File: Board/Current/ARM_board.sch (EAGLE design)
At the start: 180 parts, among them IC3 STM32F437VI, IC4 LM358DT, J1 USART/I2C, J10 ANALOG, J11 DGND, J12 DPWR, J13 DIGITAL, J14 SGND, J15 SPWR, J16 SERVO, J2 I2C2/USART3, J3 USART2, J5 SPI, J6 Bluesmirf, J7 SWD, J8 AGND, J9 APWR, Q1 STL4P2UH7, Q2 2STR1230, Q3 STL4P2UH7, SW1 SW, U1 LSM330, U10 BAV99, U11 BAV99, U12 USBLC6-2, U13 USBLC6-2, U14 STMPS2171MTR, U15 MC74HC164, U3 NC7SZU04, U4 L6206Q, U5 L6206Q, U6 SI7617, U7 SI7617, U8 SI7617, U9 SI7617, Y2 8MHz

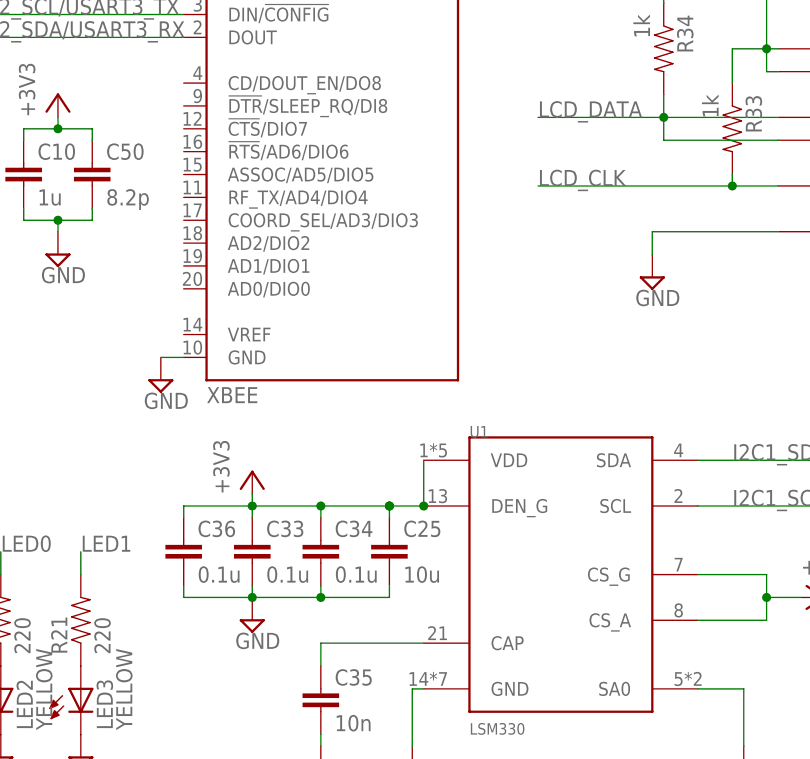
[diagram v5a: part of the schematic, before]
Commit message: Cleaned up the layout around the gyro a bit.
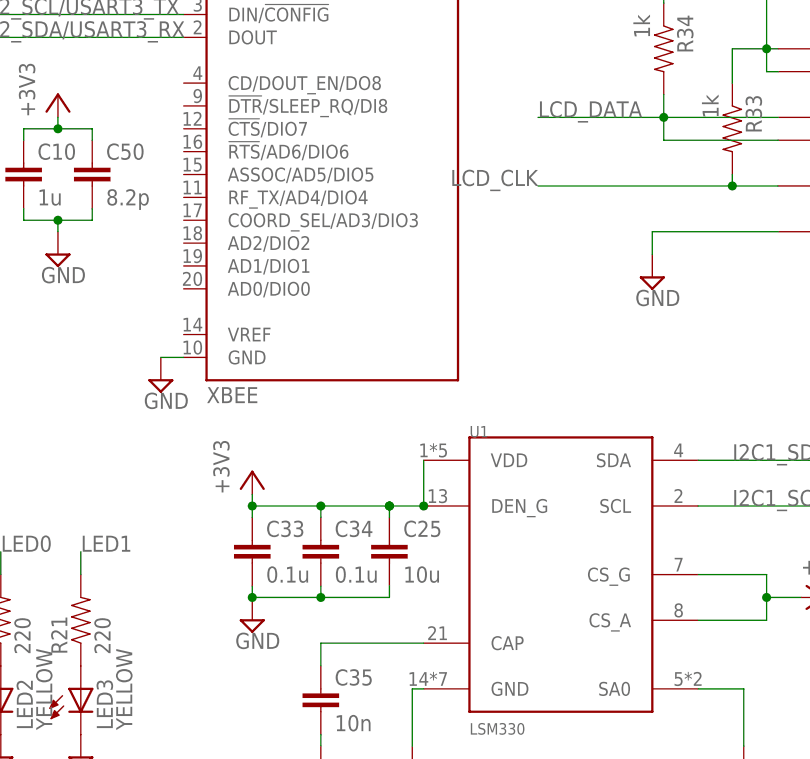
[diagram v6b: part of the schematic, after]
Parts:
- removed C36: 0.1u, SparkFun:CAP0402-CAP
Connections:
- net +3V3: no longer C36.1
- net GND: no longer C36.2
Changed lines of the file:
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@@
 <setting verticaltext="up"/>
 </settings>
-<grid distance="0.05" unitdist="inch" unit="inch" style="lines" multiple="1" display="no" altdistance="0.01" altunitdist="inch" altunit="inch"/>
+<grid distance="0.1" unitdist="inch" unit="inch" style="lines" multiple="1" display="no" altdistance="0.01" altunitdist="inch" altunit="inch"/>
 <layers>
 <layer number="1" name="Top" color="4" fill="1" visible="no" active="no"/>
@@
 <part name="R53" library="SparkFun" deviceset="RESISTOR" device="0402-RES" value="330k"/>
 <part name="C33" library="SparkFun" deviceset="CAP" device="0402-CAP" value="0.1u"/>
-<part name="C36" library="SparkFun" deviceset="CAP" device="0402-CAP" value="0.1u"/>
 </parts>
 <sheets>
@@
 <instance part="R53" gate="G$1" x="80.01" y="233.68"/>
 <instance part="C33" gate="G$1" x="261.62" y="82.55"/>
-<instance part="C36" gate="G$1" x="254" y="82.55"/>
 </instances>
 <busses>
@@
 <pinref part="C34" gate="G$1" pin="2"/>
 <wire x1="269.24" y1="80.01" x2="269.24" y2="78.74" width="0.1524" layer="91"/>
-<pinref part="C36" gate="G$1" pin="2"/>
-<wire x1="261.62" y1="78.74" x2="254" y2="78.74" width="0.1524" layer="91"/>
-<wire x1="254" y1="78.74" x2="254" y2="80.01" width="0.1524" layer="91"/>
 <junction x="261.62" y="78.74"/>
 <junction x="269.24" y="78.74"/>
@@
 <wire x1="269.24" y1="88.9" x2="261.62" y2="88.9" width="0.1524" layer="91"/>
 <wire x1="261.62" y1="88.9" x2="261.62" y2="87.63" width="0.1524" layer="91"/>
-<pinref part="C36" gate="G$1" pin="1"/>
-<wire x1="261.62" y1="88.9" x2="254" y2="88.9" width="0.1524" layer="91"/>
-<wire x1="254" y1="88.9" x2="254" y2="87.63" width="0.1524" layer="91"/>
 <junction x="261.62" y="88.9"/>
 <junction x="269.24" y="88.9"/>
@@
 <pinref part="U15" gate="G$1" pin="CLK"/>
 <wire x1="320.04" y1="124.46" x2="314.96" y2="124.46" width="0.1524" layer="91"/>
-<label x="293.37" y="124.46" size="1.778" layer="95"/>
+<label x="293.37" y="124.46" size="1.778" layer="95" rot="MR0"/>
 <pinref part="R33" gate="G$1" pin="2"/>
 <wire x1="314.96" y1="124.46" x2="293.37" y2="124.46" width="0.1524" layer="91"/>

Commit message: Cleaned up the part numbers of everything but the resistors/caps.
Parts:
- removed IC3: STM32F437VI, new_parts:STM32F407VET
- removed JP2: DPWR_SEL, SparkFun:JUMPER-3PTH
- removed JP3: MISC, SparkFun:M081X08
- removed U$1: PM6685, r_cubed:PM6685
- removed U$2: DUAL-MOSFET, r_cubed:DUAL-MOSFET
- removed U$5: LD1117V33, r_cubed:LD1117
- removed U13: USBLC6-2, new_parts:USBLC6-2
- removed U14: STMPS2171MTR, r_cubed:RT9715
- removed U15: MC74HC164, r_cubed:MC74HC164
- added D4, D5: BAV99, Parts:BAV99
- added J17: SERVO, SparkFun:M081X08
- added J4: I2C2/USART3, SparkFun:M04PTH
- added Q5, Q6: STL4P2UH7, r_cubed:STL4P2UH7
- added Q7, Q8: SI7617, r_cubed:SI7617
- added Q9: 2STR1230, SparkFun:TRANSISTOR_NPNSOT23-3
- D1: value STPS1L30M -> SOD-23; device SparkFun:DIODE-SCHOTTKYA -> r_cubed:SOD-23
- D3: value SOD-23 -> STPS1L30M; device r_cubed:SOD-23 -> SparkFun:DIODE-SCHOTTKYA
- J1: value USART/I2C -> Bluesmirf; device SparkFun:M04PTH -> SparkFun:M06SIP
- J10: value ANALOG -> APWR
- J11: value DGND -> ANALOG; device SparkFun:M15 -> SparkFun:M081X08
- J12: value DPWR -> DGND
- J13: value DIGITAL -> DPWR
- J14: value SGND -> DIGITAL; device SparkFun:M081X08 -> SparkFun:M15
- J15: value SPWR -> SGND
- J16: value SERVO -> SPWR
- J2: value I2C2/USART3 -> I2C1
- J3: value USART2 -> USART/I2C
- J6: value Bluesmirf -> USART2; device SparkFun:M06SIP -> SparkFun:M04PTH
- J8: value AGND -> MISC
- J9: value APWR -> AGND
- JP1: value I2C1 -> DPWR_SEL; device SparkFun:M04PTH -> SparkFun:JUMPER-3PTH
- Q1: value STL4P2UH7 -> SI7617; device r_cubed:STL4P2UH7 -> r_cubed:SI7617
- Q2: value 2STR1230 -> SI7617; device SparkFun:TRANSISTOR_NPNSOT23-3 -> r_cubed:SI7617
- Q3: value STL4P2UH7 -> DUAL-MOSFET; device r_cubed:STL4P2UH7 -> r_cubed:DUAL-MOSFET
- U1: value LSM330 -> PM6685; device r_cubed:LSM330 -> r_cubed:PM6685
- U10: value BAV99 -> STM32F437VI; device Parts:BAV99 -> new_parts:STM32F407VET
- U11: value BAV99 -> LSM330; device Parts:BAV99 -> r_cubed:LSM330
- U12: value USBLC6-2 -> MC74HC164; device new_parts:USBLC6-2 -> r_cubed:MC74HC164
- U3: value NC7SZU04 -> LD1117V33; device SparkFun:INVERTER"" -> r_cubed:LD1117
- U4: value L6206Q -> USBLC6-2; device r_cubed:L6206Q -> new_parts:USBLC6-2
- U5: value L6206Q -> STMPS2171MTR; device r_cubed:L6206Q -> r_cubed:RT9715
- U6: value SI7617 -> USBLC6-2; device r_cubed:SI7617 -> new_parts:USBLC6-2
- U7: value SI7617 -> NC7SZU04; device r_cubed:SI7617 -> SparkFun:INVERTER""
- U8, U9: value SI7617 -> L6206Q; device r_cubed:SI7617 -> r_cubed:L6206Q
- renumbered IC4 to U2, L3 to L2, LED2 to D9, LED3 to D10, LED4 to D8, LED5 to D11, LED6 to D7, LED7 to D6, SD to USD, SG1 to LS1, U$4 to Q4, Y2 to Y1
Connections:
- net +3V3: now also J1.5, J10.1, J10.2, J10.3, J10.4, J10.5, J10.6, J10.7, J10.8, J4.4, J6.4, JP1.1, U1.OUT3, U10BAT_AN.VBAT, U10BAT_AN.VDDA, U10BAT_AN.VDD_6, U10BAT_AN.VREF+, U10POWER.VDD_1, U10POWER.VDD_2, U10POWER.VDD_3, U10POWER.VDD_4, U10POWER.VDD_5, U11.CS_A, U11.CS_G, U11.DEN_G, U11.VDD, U12./RST, U12.VCC, U3.VOUT, U4.VBUS, U6.VBUS; no longer IC3BAT_AN.VBAT, IC3BAT_AN.VDDA, IC3BAT_AN.VDD_6, IC3BAT_AN.VREF+, IC3POWER.VDD_1, IC3POWER.VDD_2, IC3POWER.VDD_3, IC3POWER.VDD_4, IC3POWER.VDD_5, J1.4, J6.5, J9.1, J9.2, J9.3, J9.4, J9.5, J9.6, J9.7, J9.8, JP1.4, JP2.1, U$1.OUT3, U$5.VOUT, U1.CS_A, U1.CS_G, U1.DEN_G, U1.VDD, U12.VBUS, U13.VBUS, U15./RST, U15.VCC
- net 5V: now also J8.6, JP1.3, Q5.S, Q6.S, Q7.D, U1.OUT5, U5.VIN, U7.VCC; no longer JP2.3, JP3.6, Q1.S, Q3.S, U$1.OUT5, U14.VIN, U3.VCC, U9.D
- net ANALOG0: now also J11.1, U10PORTA_L.PA3; no longer IC3PORTA_L.PA3, J10.1
- net ANALOG1: now also J11.2, U10PORTA_L.PA2; no longer IC3PORTA_L.PA2, J10.2
- net ANALOG2: now also J11.3, U10PORTA_L.PA1; no longer IC3PORTA_L.PA1, J10.3
- net ANALOG3: now also J11.4, U10PORTA_L.PA0; no longer IC3PORTA_L.PA0, J10.4
- net ANALOG4: now also J11.5, U10PORTC_L.PC3; no longer IC3PORTC_L.PC3, J10.5
- net ANALOG5: now also J11.6, U10PORTC_L.PC2; no longer IC3PORTC_L.PC2, J10.6
- net ANALOG6: now also J11.7, U10PORTC_L.PC1; no longer IC3PORTC_L.PC1, J10.7
- net ANALOG7: now also J11.8, U10PORTC_L.PC0; no longer IC3PORTC_L.PC0, J10.8
- net ANALOG8: now also J8.3, U10PORTB_L.PB1; no longer IC3PORTB_L.PB1, JP3.3
- net ANALOG9: now also J8.4, U10PORTB_L.PB0; no longer IC3PORTB_L.PB0, JP3.4
- net BAT_SENSE: now also U10PORTC_L.PC4; no longer IC3PORTC_L.PC4
- net BOOT1: now also U10PORTB_L.PB2; no longer IC3PORTB_L.PB2
- net BOOT3: now also D1.P$2; no longer D3.P$2
- net BTN0: now also U10PORTD_H.PD10; no longer IC3PORTD_H.PD10
- net BTN1: now also U10PORTD_H.PD11; no longer IC3PORTD_H.PD11
- net BUZZER: now also U10PORTA_L.PA4; no longer IC3PORTA_L.PA4
- net DIGITAL0: now also J14.1, U10PORTC_H.PC15; no longer IC3PORTC_H.PC15, J13.1
- net DIGITAL1: now also J14.2, U10PORTC_H.PC14; no longer IC3PORTC_H.PC14, J13.2
- net DIGITAL10: now also J14.11, U10PORTB_L.PB5; no longer IC3PORTB_L.PB5, J13.11
- net DIGITAL11: now also J14.12, U10PORTB_L.PB4; no longer IC3PORTB_L.PB4, J13.12
- net DIGITAL12: now also J14.13, U10PORTB_L.PB3; no longer IC3PORTB_L.PB3, J13.13
- net DIGITAL13: now also J14.14, U10PORTD_L.PD7; no longer IC3PORTD_L.PD7, J13.14
- net DIGITAL14: now also J14.15, U10PORTD_L.PD3; no longer IC3PORTD_L.PD3, J13.15
- net DIGITAL15: now also J8.1, U10PORTE_H.PE13; no longer IC3PORTE_H.PE13, JP3.1
- net DIGITAL16: now also J8.2, U10PORTE_H.PE14; no longer IC3PORTE_H.PE14, JP3.2
- net DIGITAL2: now also J14.3, U10PORTC_H.PC13; no longer IC3PORTC_H.PC13, J13.3
- net DIGITAL3: now also J14.4, U10PORTE_L.PE6; no longer IC3PORTE_L.PE6, J13.4
- net DIGITAL4: now also J14.5, U10PORTE_L.PE5; no longer IC3PORTE_L.PE5, J13.5
- net DIGITAL5: now also J14.6, U10PORTE_L.PE4; no longer IC3PORTE_L.PE4, J13.6
- net DIGITAL6: now also J14.7, U10PORTE_L.PE3; no longer IC3PORTE_L.PE3, J13.7
- net DIGITAL7: now also J14.8, U10PORTE_L.PE2; no longer IC3PORTE_L.PE2, J13.8
- net DIGITAL8: now also J14.9, U10PORTE_L.PE1; no longer IC3PORTE_L.PE1, J13.9
- net DIGITAL9: now also J14.10, U10PORTE_L.PE0; no longer IC3PORTE_L.PE0, J13.10
- net GND: now also D3.A, J1.4, J12.1, J12.10, J12.11, J12.12, J12.13, J12.14, J12.15, J12.2, J12.3, J12.4, J12.5, J12.6, J12.7, J12.8, J12.9, J15.1, J15.2, J15.3, J15.4, J15.5, J15.6, J15.7, J15.8, J4.3, J6.3, J9.1, J9.2, J9.3, J9.4, J9.5, J9.6, J9.7, J9.8, Q3.S2, Q9.E, U1.LDO3SEL, U1.PGND, U1.SGND, U1.SGND2, U1.SKIP, U1.V5SW, U10BAT_AN.VSSA, U10POWER.VSS_2, U10POWER.VSS_4, U10POWER.VSS_5, U10POWER.VSS_6, U11.GND, U11.SA0, U6.GND, U7.GND, U8.GND, U8.PROGCLA, U8.PROGCLB, U8.SENSE_A, U8.SENSE_B, U9.GND, U9.PROGCLA, U9.PROGCLB, U9.SENSE_A, U9.SENSE_B; no longer D1.A, IC3BAT_AN.VSSA, IC3POWER.VSS_2, IC3POWER.VSS_4, IC3POWER.VSS_5, IC3POWER.VSS_6, J1.3, J11.1, J11.10, J11.11, J11.12, J11.13, J11.14, J11.15, J11.2, J11.3, J11.4, J11.5, J11.6, J11.7, J11.8, J11.9, J14.1, J14.2, J14.3, J14.4, J14.5, J14.6, J14.7, J14.8, J6.4, J8.1, J8.2, J8.3, J8.4, J8.5, J8.6, J8.8, JP1.3, JP3.7, Q2.E, U$1.LDO3SEL, U$1.PGND, U$1.SGND, U$1.SGND2, U$1.SKIP, U$1.V5SW, U$2.S2, U$5.GND, U1.GND, U1.SA0, U13.GND, U14.GND, U15.GND, U4.PROGCLA, U4.PROGCLB, U4.SENSE_A, U4.SENSE_B, U5.PROGCLA, U5.PROGCLB, U5.SENSE_A, U5.SENSE_B
- net I2C1_SCL: now also J2.1, U10PORTB_H.PB8, U11.SCL; no longer IC3PORTB_H.PB8, JP1.1, U1.SCL
- net I2C1_SDA: now also J2.2, U10PORTB_H.PB9, U11.SDA; no longer IC3PORTB_H.PB9, JP1.2, U1.SDA
- net I2C2_SCL/USART3_TX: now also J3.1, J4.1, U10PORTB_H.PB10; no longer IC3PORTB_H.PB10, J1.1, J2.1
- net I2C2_SDA/USART3_RX: now also J3.2, J4.2, U10PORTB_H.PB11; no longer IC3PORTB_H.PB11, J1.2, J2.2
- net LCD_CLK: now also U10PORTA_H.PA10, U12.CLK; no longer IC3PORTA_H.PA10, U15.CLK
- net LCD_DATA: now also U10PORTA_H.PA8, U12.A1, U12.A2; no longer IC3PORTA_H.PA8, U15.A1, U15.A2
- net LCD_E: now also U10PORTD_L.PD0; no longer IC3PORTD_L.PD0
- net LCD_RS: now also U10PORTD_L.PD1; no longer IC3PORTD_L.PD1
- net LDO5: now also D1.P$0, U1.FSEL, U1.LDO5; no longer D3.P$0, U$1.FSEL, U$1.LDO5
- net LED0: now also U10PORTE_H.PE15; no longer IC3PORTE_H.PE15
- net LED1: now also U10PORTD_L.PD4; no longer IC3PORTD_L.PD4
- net M0_A: now also U10PORTE_L.PE7, U8.IN1A, U8.IN1B; no longer IC3PORTE_L.PE7, U4.IN1A, U4.IN1B
- net M0_B: now also U10PORTE_H.PE8, U8.IN2A, U8.IN2B; no longer IC3PORTE_H.PE8, U4.IN2A, U4.IN2B
- net M0_EN: now also U10PORTE_H.PE9, U8.ENA, U8.ENB; no longer IC3PORTE_H.PE9, U4.ENA, U4.ENB
- net M0_FAULT: now also U10PORTD_H.PD8, U8.FAULT_A, U8.FAULT_B; no longer IC3PORTD_H.PD8, U4.FAULT_A, U4.FAULT_B
- net M1_A: now also U10PORTE_H.PE10, U9.IN1A, U9.IN1B; no longer IC3PORTE_H.PE10, U5.IN1A, U5.IN1B
- net M1_B: now also U10PORTE_H.PE12, U9.IN2A, U9.IN2B; no longer IC3PORTE_H.PE12, U5.IN2A, U5.IN2B
- net M1_EN: now also U10PORTE_H.PE11, U9.ENA, U9.ENB; no longer IC3PORTE_H.PE11, U5.ENA, U5.ENB
- net M1_FAULT: now also U10PORTD_H.PD9, U9.FAULT_A, U9.FAULT_B; no longer IC3PORTD_H.PD9, U5.FAULT_A, U5.FAULT_B
- net N$1: now also Q1.D; no longer U6.D
- net N$11: now also U11.CAP; no longer U1.CAP
- net N$13: now also U4.IO2_1; no longer U12.IO2_1
- net N$14: now also Q5.G, Q6.G; no longer Q1.G, Q3.G
- net N$15: now also U1.VCC; no longer U$1.VCC
- net N$16: now also U4.IO1_1; no longer U12.IO1_1
- net N$17: now also U6.IO1_1; no longer U13.IO1_1
- net N$19: now also J13.1, J13.10, J13.11, J13.12, J13.13, J13.14, J13.15, J13.2, J13.3, J13.4, J13.5, J13.6, J13.7, J13.8, J13.9, JP1.2; no longer J12.1, J12.10, J12.11, J12.12, J12.13, J12.14, J12.15, J12.2, J12.3, J12.4, J12.5, J12.6, J12.7, J12.8, J12.9, JP2.2
- net N$2: now also Q1.G; no longer U6.G
- net N$20: now also U1.BOOT5; no longer U$1.BOOT5
- net N$21: now also U5.VOUT; no longer U14.VOUT
- net N$22: now also Q6.D, U3.VIN; no longer Q3.D, U$5.VIN
- net N$23: now also Q1.S, Q2.S; no longer U6.S, U7.S
- net N$24: now also U10POWER.VCAP_1; no longer IC3POWER.VCAP_1
- net N$25: now also D1.P$1; no longer D3.P$1
- net N$27: now also U7.A; no longer U3.A
- net N$28: now also Q9.C; no longer Q2.C
- net N$3: now also U10RESET.BOOT0; no longer IC3RESET.BOOT0
- net N$30: now also U7.Y; no longer U3.Y
- net N$32: now also Q5.D; no longer Q1.D
- net N$33: now also U6.IO2_2; no longer U13.IO2_2
- net N$34: now also U4.IO2_2; no longer U12.IO2_2
- net N$36: now also U4.IO1_2; no longer U12.IO1_2
- net N$38: now also U9.VCP; no longer U5.VCP
- net N$39: now also D5.3, U9.VBOOT; no longer U10.3, U5.VBOOT
- net N$4: now also U10BAT_AN.VCAP_2; no longer IC3BAT_AN.VCAP_2
- net N$40: now also D5.2; no longer U10.2
- net N$44: now also U1.LGATE3; no longer U$1.LGATE3
- net N$45: now also U8.VCP; no longer U4.VCP
- net N$46: now also U10OSC.OSC_IN; no longer IC3OSC.OSC_IN
- net N$47: now also U10OSC.OSC_OUT; no longer IC3OSC.OSC_OUT
- net N$48: now also D4.3, U8.VBOOT; no longer U11.3, U4.VBOOT
- net N$49: now also D4.2; no longer U11.2
- net N$50: now also Q7.G; no longer U9.G
- net N$53: now also Q8.G; no longer U8.G
- net N$55: now also U1.CSENSE5; no longer U$1.CSENSE5
- net N$56: now also Q3.G1, U1.HGATE5; no longer U$1.HGATE5, U$2.G1
- net N$57: now also Q3.G2, U1.LGATE5; no longer U$1.LGATE5, U$2.G2
- net N$58: now also U12.QA; no longer U15.QA
- net N$59: now also U1.BOOT3; no longer U$1.BOOT3
- net N$6: now also U6.IO1_2; no longer U13.IO1_2
- net N$60: now also U12.QB; no longer U15.QB
- net N$61: now also U12.QC; no longer U15.QC
- net N$62: now also U12.QD; no longer U15.QD
- net N$63: now also U12.QE; no longer U15.QE
- net N$64: now also U12.QF; no longer U15.QF
- net N$65: now also Q9.B; no longer Q2.B
- net N$66: now also D2.C, Q3.S1, U1.PHASE5; no longer D1.C, U$1.PHASE5, U$2.S1
- net N$68: now also Q2.G; no longer U7.G
- net N$69: now also U1.COMP5; no longer U$1.COMP5
- net N$7: now also U1.VREF; no longer U$1.VREF
- net N$70: now also U12.QG; no longer U15.QG
- net N$71: now also U12.QH; no longer U15.QH
- net N$73: now also U1.HGATE3; no longer U$1.HGATE3
- net N$75: now also D3.C, U1.PHASE3; no longer D2.C, U$1.PHASE3
- net N$76: now also U1.CSENSE3; no longer U$1.CSENSE3
- net N$77: now also U1.COMP3; no longer U$1.COMP3
- net N$79: now also U1.VIN; no longer U$1.VIN
- net N$8: now also U6.IO2_1; no longer U13.IO2_1
- net N$82: now also U1.SHUDN; no longer U$1.SHUDN
- net N$83: now also U1.EN3; no longer U$1.EN3
- net N$84: now also U1.EN5; no longer U$1.EN5
- net OUT1: now also U8.OUT1A, U8.OUT1B; no longer U4.OUT1A, U4.OUT1B
- net OUT2: now also U8.OUT2A, U8.OUT2B; no longer U4.OUT2A, U4.OUT2B
- net OUT3: now also U9.OUT1A, U9.OUT1B; no longer U5.OUT1A, U5.OUT1B
- net OUT4: now also U9.OUT2A, U9.OUT2B; no longer U5.OUT2A, U5.OUT2B
- net RAW_SPWR: now also Q8.D; no longer U8.D
- net RESET: now also J8.5, U10RESET.NRST; no longer IC3RESET.NRST, JP3.5
- net SERVO0: now also J17.8, U10PORTD_H.PD12; no longer IC3PORTD_H.PD12, J16.8
- net SERVO1: now also J17.7, U10PORTD_H.PD13; no longer IC3PORTD_H.PD13, J16.7
- net SERVO2: now also J17.6, U10PORTD_H.PD14; no longer IC3PORTD_H.PD14, J16.6
- net SERVO3: now also J17.5, U10PORTD_H.PD15; no longer IC3PORTD_H.PD15, J16.5
- net SERVO4: now also J17.4, U10PORTC_L.PC6; no longer IC3PORTC_L.PC6, J16.4
- net SERVO5: now also J17.3, U10PORTC_L.PC7; no longer IC3PORTC_L.PC7, J16.3
- net SERVO6: now also J17.2, U10PORTC_H.PC8; no longer IC3PORTC_H.PC8, J16.2
- net SERVO7: now also J17.1, U10PORTC_H.PC9; no longer IC3PORTC_H.PC9, J16.1
- net SERVO_SENSE: now also U10PORTC_L.PC5; no longer IC3PORTC_L.PC5
- net SPI1_MISO: now also U10PORTA_L.PA6; no longer IC3PORTA_L.PA6
- net SPI1_MOSI: now also U10PORTA_L.PA7; no longer IC3PORTA_L.PA7
- net SPI1_NSS: now also U10PORTA_H.PA15; no longer IC3PORTA_H.PA15
- net SPI1_SCK: now also U10PORTA_L.PA5; no longer IC3PORTA_L.PA5
- net SPI3_MISO: now also U10PORTC_H.PC11; no longer IC3PORTC_H.PC11
- net SPI3_MOSI: now also U10PORTC_H.PC12; no longer IC3PORTC_H.PC12
- net SPI3_NSS: now also U10PORTD_L.PD2; no longer IC3PORTD_L.PD2
- net SPI3_SCK: now also U10PORTC_H.PC10; no longer IC3PORTC_H.PC10
- net SPWR: now also J16.1, J16.2, J16.3, J16.4, J16.5, J16.6, J16.7, J16.8, Q7.S, Q8.S; no longer J15.1, J15.2, J15.3, J15.4, J15.5, J15.6, J15.7, J15.8, U8.S, U9.S
- net SWDCLK: now also U10PORTA_H.PA14; no longer IC3PORTA_H.PA14
- net SWDIO: now also U10PORTA_H.PA13; no longer IC3PORTA_H.PA13
- net USART1_RX: now also J1.3, U10PORTB_L.PB7; no longer IC3PORTB_L.PB7, J6.3
- net USART1_TX: now also J1.2, U10PORTB_L.PB6; no longer IC3PORTB_L.PB6, J6.2
- net USART2_RX: now also J6.2, U10PORTD_L.PD6; no longer IC3PORTD_L.PD6, J3.2
- net USART2_TX: now also J6.1, U10PORTD_L.PD5; no longer IC3PORTD_L.PD5, J3.1
- net USB_5V: now also U10PORTA_H.PA9; no longer IC3PORTA_H.PA9
- net USB_DEV_DM: now also U10PORTA_H.PA11; no longer IC3PORTA_H.PA11
- net USB_DEV_DP: now also U10PORTA_H.PA12; no longer IC3PORTA_H.PA12
- net USB_HOST_DM: now also U10PORTB_H.PB14; no longer IC3PORTB_H.PB14
- net USB_HOST_DP: now also U10PORTB_H.PB15; no longer IC3PORTB_H.PB15
- net USB_HOST_EN: now also U10PORTB_H.PB13, U5.EN; no longer IC3PORTB_H.PB13, U14.EN
- net USB_HOST_FAULT: now also U10PORTB_H.PB12, U5.FAULT; no longer IC3PORTB_H.PB12, U14.FAULT
- net VIN: now also D4.1, D5.1, J8.8, Q2.D, Q3.D1, U8.VS, U9.VS; no longer JP3.8, U$2.D1, U10.1, U11.1, U4.VS, U5.VS, U7.D
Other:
- note added: "D1"
- note removed: "D3"
- moved on the sheet: D2, J10, J12, J13, J15, J16, J2, J3, J8, J9, Q1

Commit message: Made some minor tweaks to the schematic and layout while creating the BOM.
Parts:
- C10, C9: device SparkFun:CAP0603-CAP -> SparkFun:CAP0402-CAP
- C11: device SparkFun:CAP0805 -> SparkFun:CAP0402-CAP
- C23, C24: device SparkFun:CAP0805 -> SparkFun:CAP0603-CAP
- C27: device SparkFun:CAP0805 -> SparkFun:CAP1206
- C39, C61: device SparkFun:CAP0402-CAP -> SparkFun:CAP0603-CAP
- C44, C52: value 680uF -> 470u
- C50: value 8.2p -> 20p
- D1: value SOD-23 -> BAS70-06FILM
- D4: value BAV99 -> BAS70-05FILM
- D6, D7: value LED_R/G -> RED/GRN
- J3: value USART/I2C -> I2C2/USART3
- U3: value LD1117V33 -> LD1117D33TR
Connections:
- net +3V3: no longer R33.1, R34.1, U12./RST, U12.VCC
- net 5V: now also R33.1, R34.1, U12./RST, U12.VCC
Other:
- moved on the sheet: D11, R35
